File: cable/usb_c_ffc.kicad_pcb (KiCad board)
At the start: 2 copper layers, 45.5 x 39.1 mm, 7 parts, among them J1 Conn_01x15_Socket, J2 Conn_01x15_Socket, J3 Conn_01x15_Socket, J4 Conn_01x15_Socket, J5 Conn_01x15_Socket, P1 TC-003LS, P2 TC-003LS

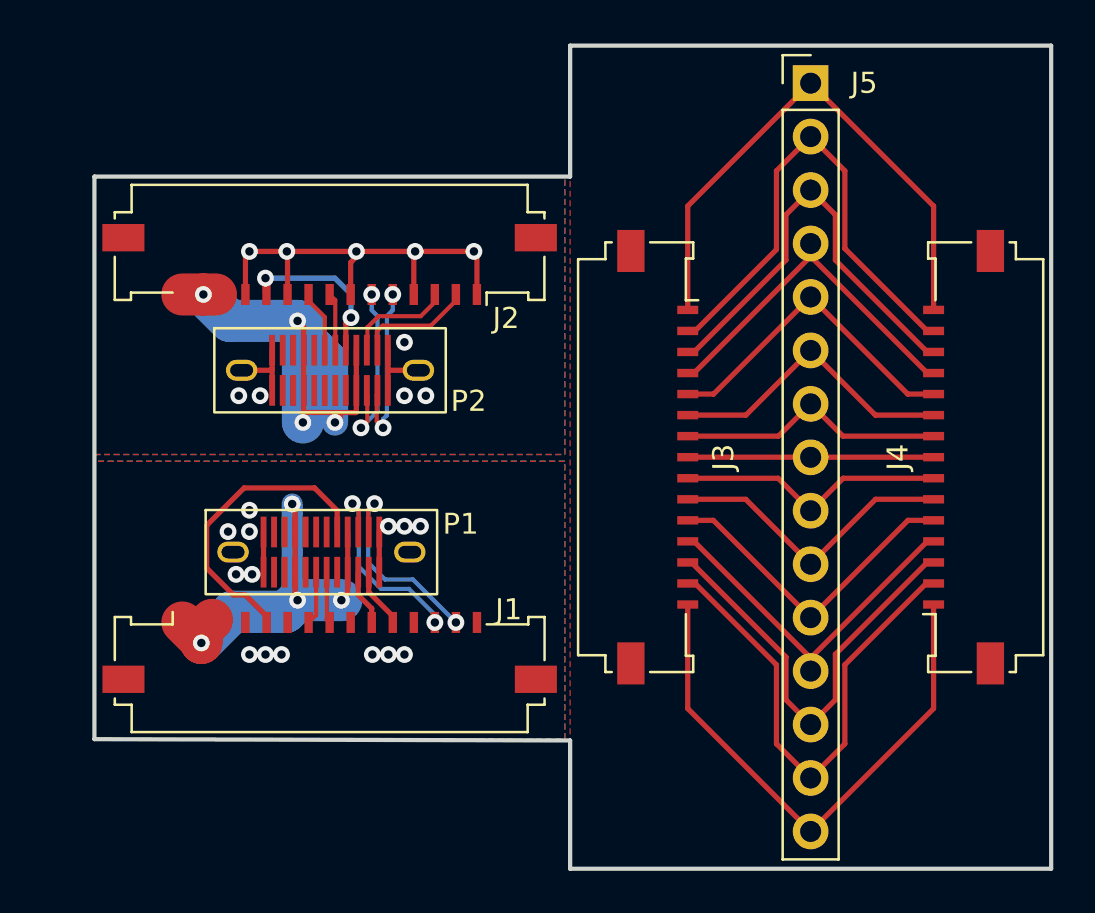
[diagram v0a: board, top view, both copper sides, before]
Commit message: use mousebites on cable instead
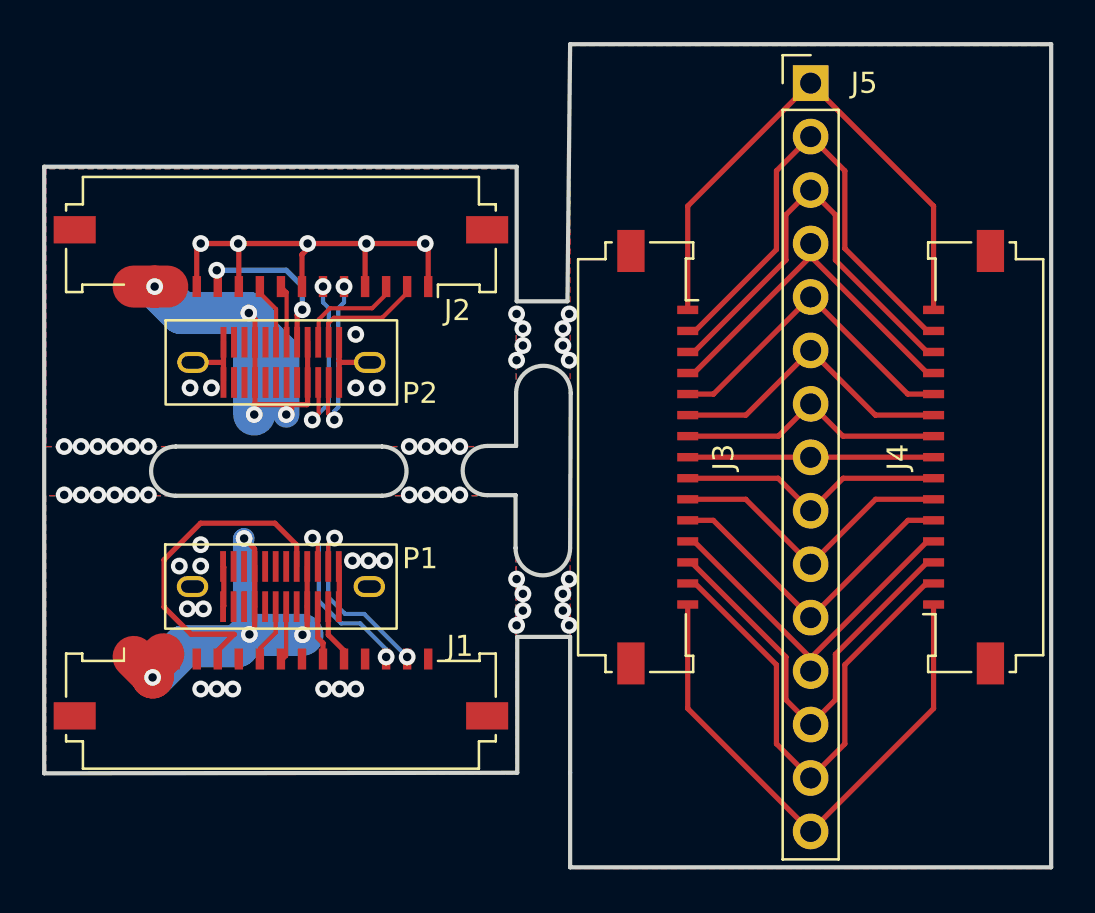
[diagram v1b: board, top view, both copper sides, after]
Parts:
- moved J1 2.90 mm to (46.2, 125.3)
- moved P1 2.53 mm to (46.2, 121.0)
- moved J2 2.34 mm to (46.2, 105.8)
- moved P2 2.34 mm to (46.2, 110.3)
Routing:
- net Net-(J1-Pin_1): track 22.9 -> 25.4 mm
- net Net-(J1-Pin_5): track 14.5 -> 16.0 mm
- net (no net): vias 0 -> 36
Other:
- board size 45.5 x 39.1 mm -> 47.9 x 39.1 mm

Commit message: ah whatever
i will just go with 3 seperate PCBs. its actually cheaper that way
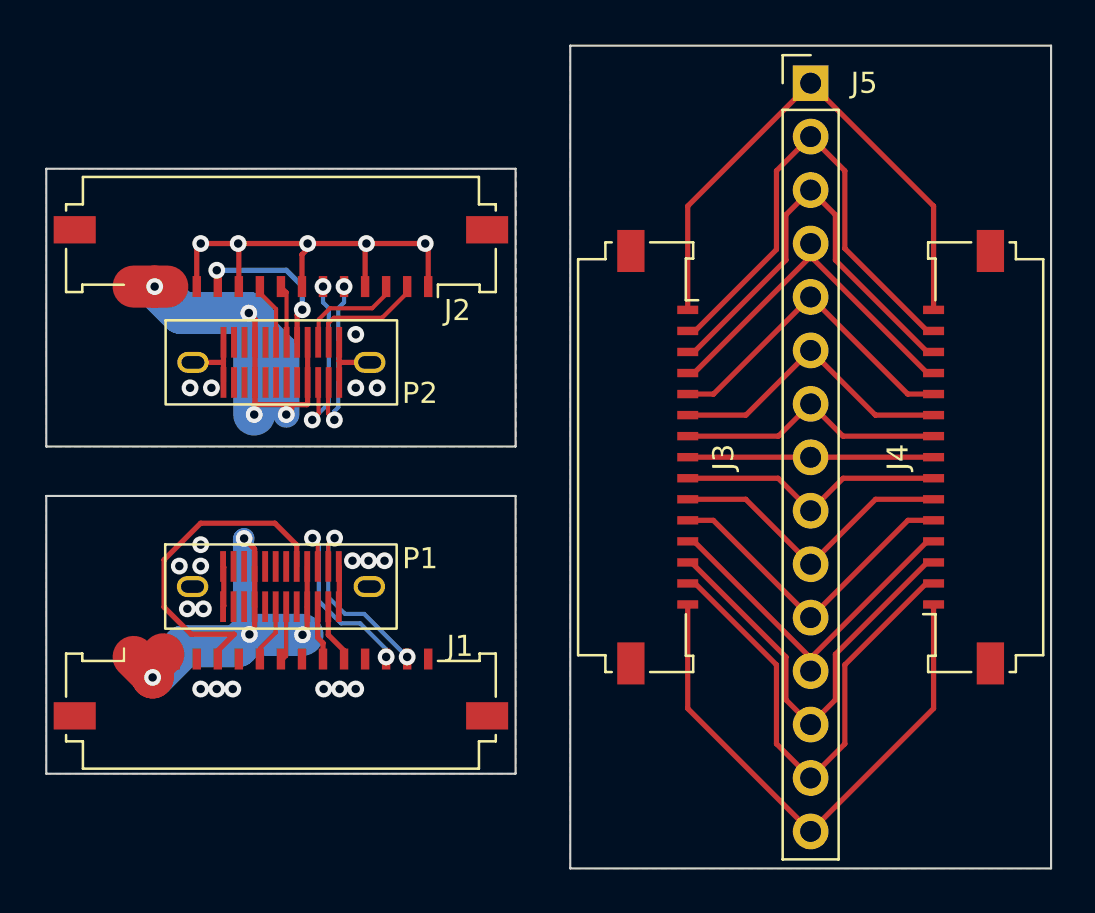
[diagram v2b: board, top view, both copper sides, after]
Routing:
- net (no net): vias 36 -> 0
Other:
- board size 47.9 x 39.1 mm -> 47.8 x 39.1 mm
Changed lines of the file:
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@@
     )
   )
-  (gr_line (start 56 114.273) (end 57.377 114.273)
-    (stroke (width 0.2) (type default)) (layer "Edge.Cuts"))
-  (gr_arc (start 57.377 111.76) (mid 58.674 110.463) (end 59.971 111.76)
-    (stroke (width 0.2) (type default)) (layer "Edge.Cuts"))
-  (gr_arc (start 51 114.3) (mid 52.17 115.47) (end 51 116.64)
-    (stroke (width 0.2) (type default)) (layer "Edge.Cuts"))
-  (gr_line (start 56.007 116.613) (end 57.35 116.613)
-    (stroke (width 0.2) (type default)) (layer "Edge.Cuts"))
-  (gr_arc (start 41.2 116.64) (mid 40.03 115.47) (end 41.2 114.3)
-    (stroke (width 0.2) (type default)) (layer "Edge.Cuts"))
-  (gr_line (start 59.971 111.76) (end 59.944 119.126)
-    (stroke (width 0.2) (type default)) (layer "Edge.Cuts"))
-  (gr_line (start 57.377 111.76) (end 57.377 114.273)
-    (stroke (width 0.2) (type default)) (layer "Edge.Cuts"))
-  (gr_line (start 41.2 116.64) (end 51 116.64)
-    (stroke (width 0.2) (type default)) (layer "Edge.Cuts"))
-  (gr_poly
-    (pts
-      (xy 59.944 123.348)
-      (xy 57.431 123.348)
-      (xy 57.431 129.80359)
-      (xy 34.95 129.831)
-      (xy 34.95 101.004)
-      (xy 57.404 101.004)
-      (xy 57.404 107.4)
-      (xy 59.817 107.4)
-      (xy 59.944 95.181)
-      (xy 82.804 95.181)
-      (xy 82.804 134.297)
-      (xy 59.944 134.297)
-      (xy 59.944 129.801)
-    )
-    (stroke (width 0.2) (type solid)) (fill none) (layer "Edge.Cuts"))
-  (gr_line (start 41.2 114.3) (end 51 114.3)
-    (stroke (width 0.2) (type default)) (layer "Edge.Cuts"))
-  (gr_arc (start 59.944 119.126) (mid 58.647 120.423) (end 57.35 119.126)
-    (stroke (width 0.2) (type default)) (layer "Edge.Cuts"))
-  (gr_line (start 57.35 119.126) (end 57.35 116.613)
-    (stroke (width 0.2) (type default)) (layer "Edge.Cuts"))
-  (gr_arc (start 56.007 116.613) (mid 54.837 115.443) (end 56.007 114.273)
-    (stroke (width 0.2) (type default)) (layer "Edge.Cuts"))
-  (via (at 57.7 109.5) (size 0.8) (drill 0.4) (layers "F.Cu" "B.Cu") (free) (net 0))
-  (via (at 53.9 114.3) (size 0.8) (drill 0.4) (layers "F.Cu" "B.Cu") (free) (net 0))
-  (via (at 59.6 109.5) (size 0.8) (drill 0.4) (layers "F.Cu" "B.Cu") (free) (net 0))
-  (via (at 39.9 116.6) (size 0.8) (drill 0.4) (layers "F.Cu" "B.Cu") (free) (net 0))
-  (via (at 39.1 116.6) (size 0.8) (drill 0.4) (layers "F.Cu" "B.Cu") (free) (net 0))
-  (via (at 37.5 114.3) (size 0.8) (drill 0.4) (layers "F.Cu" "B.Cu") (free) (net 0))
-  (via (at 54.7 114.3) (size 0.8) (drill 0.4) (layers "F.Cu" "B.Cu") (free) (net 0))
-  (via (at 59.6 108.7) (size 0.8) (drill 0.4) (layers "F.Cu" "B.Cu") (free) (net 0))
-  (via (at 59.9 120.6) (size 0.8) (drill 0.4) (layers "F.Cu" "B.Cu") (free) (net 0))
-  (via (at 39.9 114.3) (size 0.8) (drill 0.4) (layers "F.Cu" "B.Cu") (free) (net 0))
-  (via (at 57.7 121.3) (size 0.8) (drill 0.4) (layers "F.Cu" "B.Cu") (free) (net 0))
-  (via (at 39.1 114.3) (size 0.8) (drill 0.4) (layers "F.Cu" "B.Cu") (free) (net 0))
-  (via (at 57.4 110.2) (size 0.8) (drill 0.4) (layers "F.Cu" "B.Cu") (free) (net 0))
-  (via (at 59.9 108) (size 0.8) (drill 0.4) (layers "F.Cu" "B.Cu") (free) (net 0))
-  (via (at 59.9 110.2) (size 0.8) (drill 0.4) (layers "F.Cu" "B.Cu") (free) (net 0))
-  (via (at 57.4 108) (size 0.8) (drill 0.4) (layers "F.Cu" "B.Cu") (free) (net 0))
-  (via (at 53.9 116.6) (size 0.8) (drill 0.4) (layers "F.Cu" "B.Cu") (free) (net 0))
-  (via (at 59.6 122.1) (size 0.8) (drill 0.4) (layers "F.Cu" "B.Cu") (free) (net 0))
-  (via (at 37.5 116.6) (size 0.8) (drill 0.4) (layers "F.Cu" "B.Cu") (free) (net 0))
-  (via (at 59.6 121.3) (size 0.8) (drill 0.4) (layers "F.Cu" "B.Cu") (free) (net 0))
-  (via (at 59.9 122.8) (size 0.8) (drill 0.4) (layers "F.Cu" "B.Cu") (free) (net 0))
-  (via (at 57.4 120.6) (size 0.8) (drill 0.4) (layers "F.Cu" "B.Cu") (free) (net 0))
-  (via (at 35.9 116.6) (size 0.8) (drill 0.4) (layers "F.Cu" "B.Cu") (free) (net 0))
-  (via (at 36.7 114.3) (size 0.8) (drill 0.4) (layers "F.Cu" "B.Cu") (free) (net 0))
-  (via (at 54.7 116.6) (size 0.8) (drill 0.4) (layers "F.Cu" "B.Cu") (free) (net 0))
-  (via (at 53.1 114.3) (size 0.8) (drill 0.4) (layers "F.Cu" "B.Cu") (free) (net 0))
-  (via (at 38.3 114.3) (size 0.8) (drill 0.4) (layers "F.Cu" "B.Cu") (free) (net 0))
-  (via (at 38.3 116.6) (size 0.8) (drill 0.4) (layers "F.Cu" "B.Cu") (free) (net 0))
-  (via (at 57.7 108.7) (size 0.8) (drill 0.4) (layers "F.Cu" "B.Cu") (free) (net 0))
-  (via (at 52.3 116.6) (size 0.8) (drill 0.4) (layers "F.Cu" "B.Cu") (free) (net 0))
-  (via (at 57.7 122.1) (size 0.8) (drill 0.4) (layers "F.Cu" "B.Cu") (free) (net 0))
-  (via (at 35.9 114.3) (size 0.8) (drill 0.4) (layers "F.Cu" "B.Cu") (free) (net 0))
-  (via (at 57.4 122.8) (size 0.8) (drill 0.4) (layers "F.Cu" "B.Cu") (free) (net 0))
-  (via (at 52.3 114.3) (size 0.8) (drill 0.4) (layers "F.Cu" "B.Cu") (free) (net 0))
-  (via (at 36.7 116.6) (size 0.8) (drill 0.4) (layers "F.Cu" "B.Cu") (free) (net 0))
-  (via (at 53.1 116.6) (size 0.8) (drill 0.4) (layers "F.Cu" "B.Cu") (free) (net 0))
+  (gr_rect (start 59.95 95.25) (end 82.8 134.35)
+    (stroke (width 0.1) (type default)) (fill none) (layer "Edge.Cuts"))
+  (gr_rect (start 35.05 101.1) (end 57.35 114.3)
+    (stroke (width 0.1) (type default)) (fill none) (layer "Edge.Cuts"))
+  (gr_rect (start 35.05 116.65) (end 57.35 129.85)
+    (stroke (width 0.1) (type default)) (fill none) (layer "Edge.Cuts"))
   (segment (start 44.95 122.982467) (end 44.702644 123.229823) (width 0.25) (layer "F.Cu") (net 1))
   (segment (start 40.102 124.681) (end 40.61 124.173) (width 2) (layer "F.Cu") (net 1))
